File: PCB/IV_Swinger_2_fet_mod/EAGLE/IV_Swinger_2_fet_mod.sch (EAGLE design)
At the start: 33 parts, among them J1 

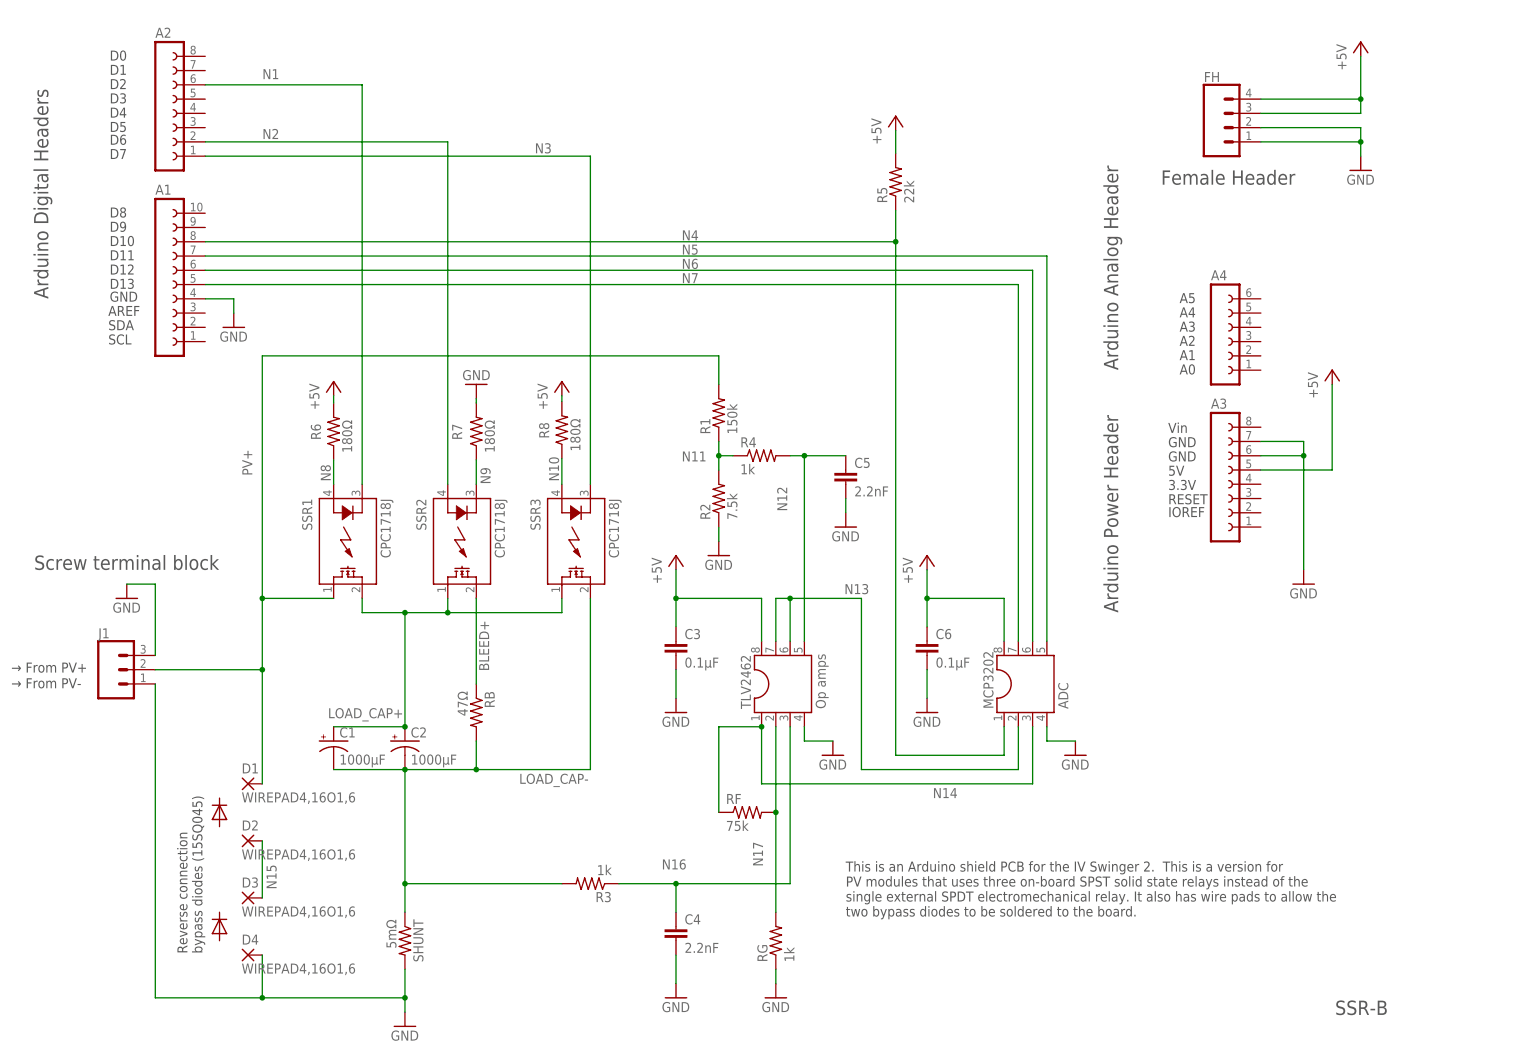
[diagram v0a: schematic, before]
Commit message: Correct EAGLE files for FET module version (Issue #218)
Replace the incorrect files with the correct ones.
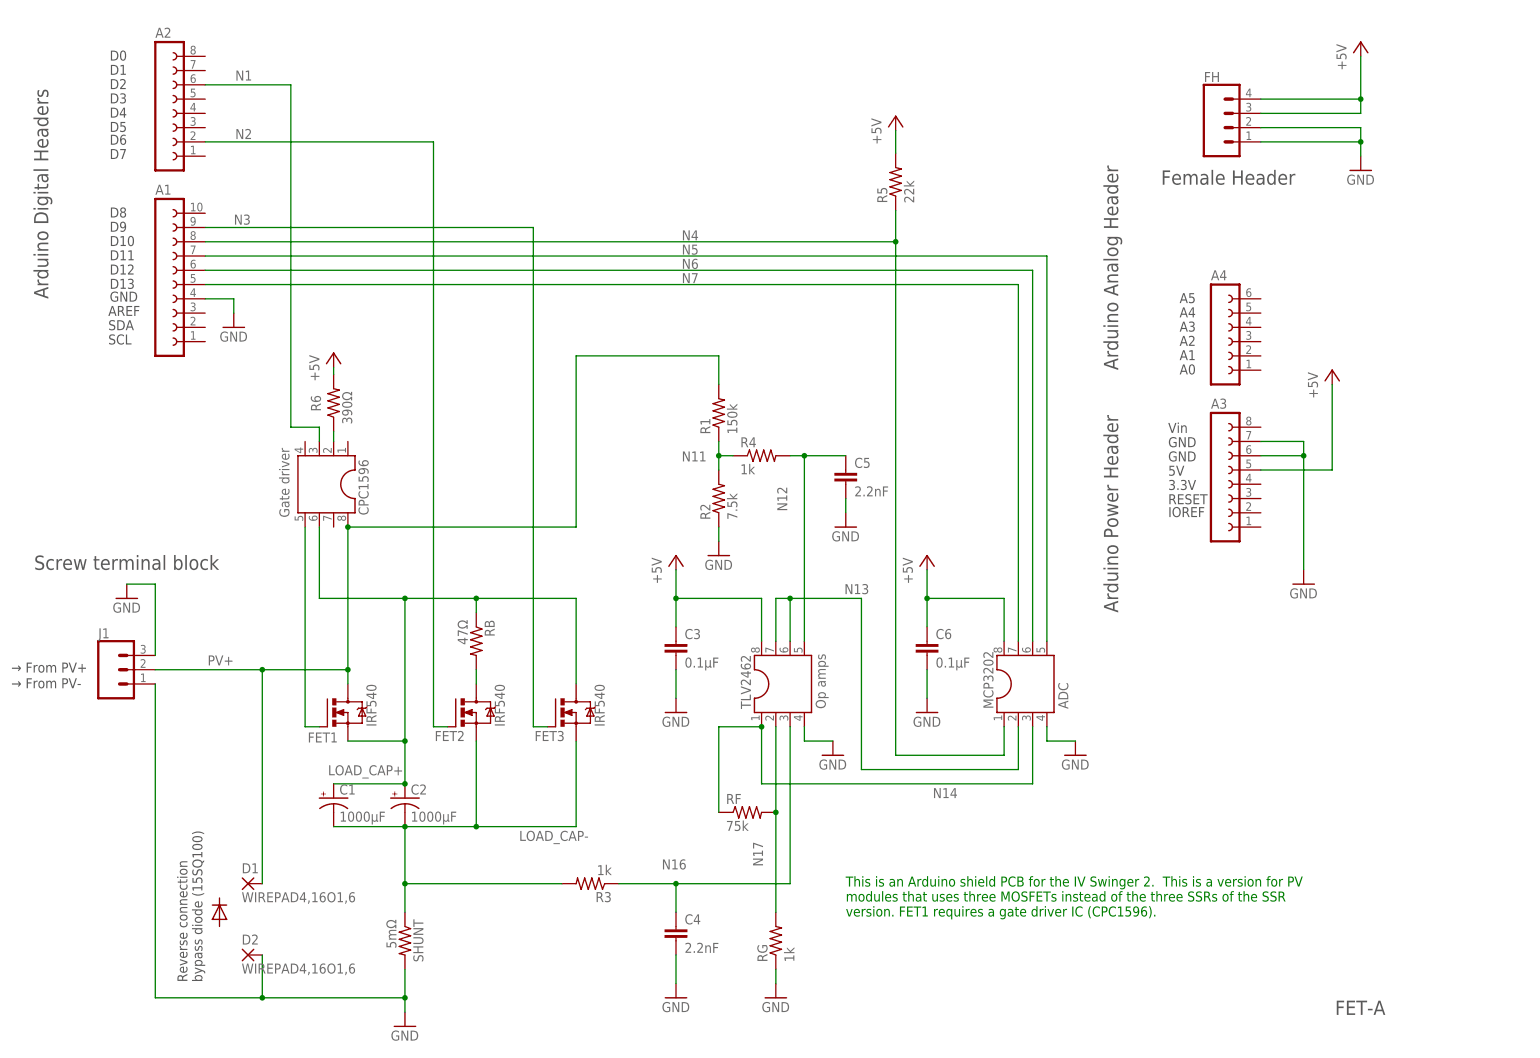
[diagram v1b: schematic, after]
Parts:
- removed D3, D4: WIREPAD4,16O1,6, wirepad:WIREPAD4,16O1,6
- removed R7, R8: 180Ω, rcl:R-US_0207/10
- removed SSR1, SSR2, SSR3: CPC1718J, my_relay:CPC1718J
- added CPC1596: Gate driver, ic-package:DIL8S
- added FET1, FET2, FET3: IRF540, transistor-power:IRF540
- R6: value 180Ω -> 390Ω
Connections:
- removed net BLEED+: RB.1, SSR2.DS2
- removed net N10: R8.1, SSR3.A
- removed net N15: D2.P, D3.P
- removed net N8: R6.1, SSR1.A
- removed net N9: R7.1, SSR2.K
- new net N$2: FET2.D, RB.2
- new net N$3: CPC1596.5, FET1.G
- new net N$4: CPC1596.2, R6.1
- net +5V: no longer R8.2
- net GND: now also D2.P; no longer D4.P, R7.2
- net LOAD_CAP+: now also CPC1596.6, FET1.S, FET3.D, RB.1; no longer SSR1.DS2, SSR2.DS1, SSR3.DS1
- net LOAD_CAP-: now also FET2.S, FET3.S; no longer RB.2, SSR3.DS2
- net N1: now also CPC1596.3; no longer SSR1.K
- net N2: now also FET2.G; no longer SSR2.A
- net N3: now also A1.9, FET3.G; no longer A2.1, SSR3.K
- net PV+: now also CPC1596.8, FET1.D; no longer SSR1.DS1
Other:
- note added: "FET-A"
- note added: "Reverse connection bypass diode (15SQ100)"
- note added: "This is an Arduino shield PCB for the IV Swinger 2. This is a version for PV modules that uses three MOSFETs instead of the three SSRs of the SSR version. FET1 requires a gate driver IC (CPC1596)."
- note removed: "Reverse connection bypass diodes (15SQ045)"
- note removed: "SSR-B"
- note removed: "This is an Arduino shield PCB for the IV Swinger 2. This is a version for PV modules that uses three on-board SPST solid state relays instead of the single external SPDT electromechanical relay. It also has wire pads to allow the two bypass diodes to be soldered to the board."
- moved on the sheet: C1, C2, D1, D2, R6, RB
